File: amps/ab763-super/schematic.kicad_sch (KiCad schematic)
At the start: 113 parts, among them T1 125P5D · 360-0-360V, T2 125C1A, T3 125A9A, T4 125A20B

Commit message: Fix: state the datasheet unit on 17 dual-triode sections whose sheets printed the other half's pin numbers
The sheet-vs-board gate reported these sockets as SECTION-SWAP; the
2026-09-10 source-read triage found the BOARD right on every one of them
(and both surfaces wrong on the 5G9 tremolo bottle). Each sheet had
lettered the section on the default map (A -> unit 1 -> pins 6/7/8) where
the factory drawing puts that stage on 1/2/3. The draw scripts now state
`unit=` on both halves, with the source cited beside the call, so the
printed socket numbers are the factory's:

- 5f4 V3: driver V3A -> 1/2/3, cathodyne V3B -> 6/7/8
  (crop 5f4-V3-layout-trace.png: +213 V driver plate -> pin 1, +270 V -> 6)
- 5f8a V3: 82k half V3A -> 1/2/3, 100k half V3B -> 6/7/8
  (crop 5f8a-V3-layout-trace.png: +225 -> 6, +19 -> 2, +28.5 -> 8)
- 6161 V1: channel 1 V1A -> 1/2/3 (crop 6161-V1-ch1.png prints 1/2/3);
  6161 V2: 1 MEG-grid half V2A -> 1/2/3, paraphase V2B -> 6/7/8
  (crop 6161-V2.png / 6161-V2-right.png)
- 6g3 V3: 82k half V3A -> 1/2/3 (crop 6g3-V3-layout-wires.png: +230 -> 1,
  +225 -> 6, +20 -> 7)
- aa1164 V3: recovery V3A -> 1/2/3, mixer V3B -> 6/7/8
  (crops aa1164-V3A-recovery-schem.png, aa1164-V3B-mixer-schem.png)
- aa864-bassman V1/V2: input stages 2/1/3, second stages 7/6/8; V4: the
  .1/500 pF-fed 82k half 2/1/3 (crops aa864-V1A-input.png,
  aa864-V1B-second.png, aa864-V2A-input.png, aa864-V2B-second.png,
  aa864-V4-PI.png)
- ab165 V1/V2/V4: same pattern (crops ab165-V1A-input.png,
  ab165-V1B-second.png, ab165-V2A-input.png, ab165-V2B-second.png,
  ab165-V4-PI.png)
- ab763-super V1/V2: slope-plate +270 V -> pin 1 (input stage), .047
  plate -> 6 (crops ab763-super-V1-layout-sh.png, ab763-super-V2-layout-sh.png)
- dr103 V2/V3: gain stages 6/7/8, cathode followers 1/2/3 (crops
  dr103-V2-huss.png, dr103-V3-huss.png — the Huss redraw, not a factory
  print; noted in the script)
- 5g9 V3: oscillator V3A -> 1/2/3, follower V3B -> 6/7/8 (crops
  5g9-V3-strap71-zoom.png, 5g9-V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
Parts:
- V1A, V2A: Basing_unit (none) -> 2
- V1B, V2B: Basing_unit (none) -> 1
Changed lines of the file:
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@@
     (in_bom yes) (on_board yes)
     (property "Reference" "V1A" (at 65.6088 33.489 0) (effects (font (size 1.27 1.27)) (justify left)))
-    (property "Value" "12AX7" (at 65.6088 35.889 0) (effects (font (size 1.27 1.27)) (justify left))))
+    (property "Value" "12AX7" (at 65.6088 35.889 0) (effects (font (size 1.27 1.27)) (justify left)))
+    (property "Basing_unit" "2" (at 65.6088 38.289 0) (effects (font (size 1.27 1.27)) hide)))
   (wire (pts (xy 47.6088 39.889) (xy 51.9888 39.889))
     (stroke (width 0) (type default)))
@@
     (in_bom yes) (on_board yes)
     (property "Reference" "V1B" (at 165.609 33.489 0) (effects (font (size 1.27 1.27)) (justify left)))
-    (property "Value" "12AX7" (at 165.609 35.889 0) (effects (font (size 1.27 1.27)) (justify left))))
+    (property "Value" "12AX7" (at 165.609 35.889 0) (effects (font (size 1.27 1.27)) (justify left)))
+    (property "Basing_unit" "1" (at 165.609 38.289 0) (effects (font (size 1.27 1.27)) hide)))
   (wire (pts (xy 147.609 39.889) (xy 151.989 39.889))
     (stroke (width 0) (type default)))
@@
     (in_bom yes) (on_board yes)
     (property "Reference" "V2A" (at 65.6088 87.489 0) (effects (font (size 1.27 1.27)) (justify left)))
-    (property "Value" "12AX7" (at 65.6088 89.889 0) (effects (font (size 1.27 1.27)) (justify left))))
+    (property "Value" "12AX7" (at 65.6088 89.889 0) (effects (font (size 1.27 1.27)) (justify left)))
+    (property "Basing_unit" "2" (at 65.6088 92.289 0) (effects (font (size 1.27 1.27)) hide)))
   (wire (pts (xy 47.6088 93.889) (xy 51.9888 93.889))
     (stroke (width 0) (type default)))
@@
     (in_bom yes) (on_board yes)
     (property "Reference" "V2B" (at 165.609 87.489 0) (effects (font (size 1.27 1.27)) (justify left)))
-    (property "Value" "12AX7" (at 165.609 89.889 0) (effects (font (size 1.27 1.27)) (justify left))))
+    (property "Value" "12AX7" (at 165.609 89.889 0) (effects (font (size 1.27 1.27)) (justify left)))
+    (property "Basing_unit" "1" (at 165.609 92.289 0) (effects (font (size 1.27 1.27)) hide)))
   (wire (pts (xy 147.609 93.889) (xy 151.989 93.889))
     (stroke (width 0) (type default)))
@@
   (polyline (pts (xy 79.7088 238.244) (xy 81.6088 236.644) (xy 87.6088 238.724) (xy 93.6088 236.644) (xy 95.5088 238.244))
     (stroke (width 0.598) (type default) (color 197 163 255 1)) (fill (type none)))
-  (text "6" (at 60.4588 33.539 0)
+  (text "1" (at 60.4588 33.539 0)
     (effects (font (size 1.1 1.1)) (justify left)))
-  (text "7" (at 52.6616 38.489 0)
+  (text "2" (at 52.6616 38.489 0)
     (effects (font (size 1.1 1.1)) (justify left)))
-  (text "8" (at 60.4588 46.239 0)
+  (text "3" (at 60.4588 46.239 0)
     (effects (font (size 1.1 1.1)) (justify left)))
-  (text "1" (at 160.459 33.539 0)
+  (text "6" (at 160.459 33.539 0)
     (effects (font (size 1.1 1.1)) (justify left)))
-  (text "2" (at 152.662 38.489 0)
+  (text "7" (at 152.662 38.489 0)
     (effects (font (size 1.1 1.1)) (justify left)))
-  (text "3" (at 160.459 46.239 0)
+  (text "8" (at 160.459 46.239 0)
     (effects (font (size 1.1 1.1)) (justify left)))
-  (text "6" (at 60.4588 87.539 0)
+  (text "1" (at 60.4588 87.539 0)
     (effects (font (size 1.1 1.1)) (justify left)))
-  (text "7" (at 52.6616 92.489 0)
+  (text "2" (at 52.6616 92.489 0)
     (effects (font (size 1.1 1.1)) (justify left)))
-  (text "8" (at 60.4588 100.239 0)
+  (text "3" (at 60.4588 100.239 0)
     (effects (font (size 1.1 1.1)) (justify left)))
-  (text "1" (at 160.459 87.539 0)
+  (text "6" (at 160.459 87.539 0)
     (effects (font (size 1.1 1.1)) (justify left)))
-  (text "2" (at 152.662 92.489 0)
+  (text "7" (at 152.662 92.489 0)
     (effects (font (size 1.1 1.1)) (justify left)))
-  (text "3" (at 160.459 100.239 0)
+  (text "8" (at 160.459 100.239 0)
     (effects (font (size 1.1 1.1)) (justify left)))
   (text "6" (at 80.4588 137.539 0)

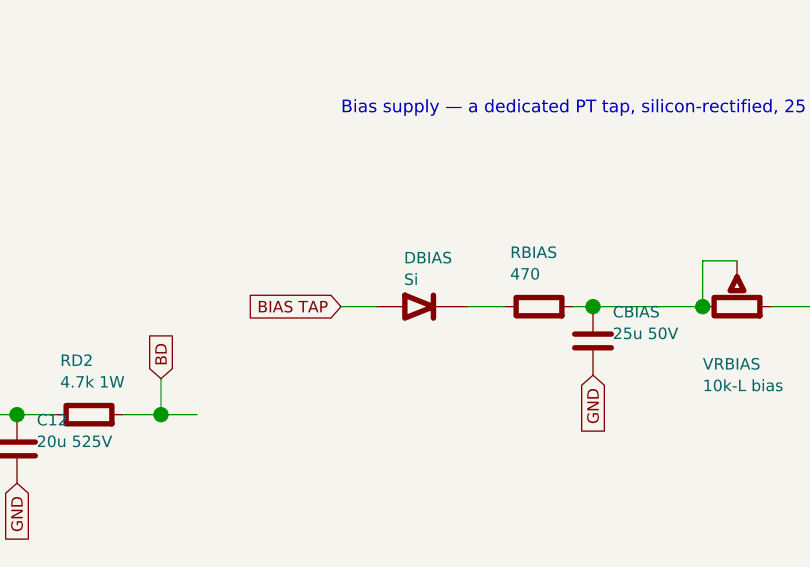
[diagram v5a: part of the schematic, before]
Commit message: Fix: 17 bias rectifiers and six HT diodes drawn backwards; the 6G6-B and 6G4 bias rows as their drawings show; AA1164 V4 units
Rectifier polarity has no gate. The netlists model every supply as an ideal
source, the sheet-vs-board check treats a two-terminal part as unordered, and
the boards' `cathode:` fields were copied from the sheets. Measured over all
68 diodes on 40 sheets: 18 negative-bias rectifiers had the cathode on the
negative node (a diode that way round would charge the node POSITIVE), and all
six 6G6-B HT diodes pointed away from B+. The printed negative bias on each of
those sheets falsifies the drawn orientation; the nine bias rectifiers already
right (AA1164, AA864, AB165, B15N, DR103, JTM100, M1959, M2204, 6G6-B) show
the idiom. Flipped: 5E4-A, 5E5-A, 5E6-A, 5F10, 5F4, 5F6, 5F6-A, 5F8-A, 5G9,
6G2, 6G3, 6G4, 6G5, AA964, AB763, AB763 Super, AB763 Twin, JTM45 (the
M1987's is with the Marshall board repair) and the 6G6-B's DR1-DR6. The
5F8-A board, which had copied its sheet, has the band moved to the tap side;
the other boards' bands are with the board-repair wave. A gate is next.

6G6-B bias. E-FB (6431x3364): the 1K 1W rises from TR1's SECOND secondary
terminal, a bias tap between the upper HT end and the grounded centre tap,
to the diode's + end. The sheet fed the diode from the HT end with the 1K
after it. T1 now carries its tap pin and the row reads tap -> 1K -> diode ->
-54 V. (The triage had read "HT end"; the native crop shows the tap.)

6G4 bias. A-FJ, read natively: tap -> rectifier -> 8 uF -> 10K -> the -55 V
node, which carries a second 8 uF and the 56K to ground as a bleeder. The
sheet fed the rectifier from an HT end, drew the 56K in series and carried
one capacitor. CBIAS2 joins the parts list, and RBIAS1's role now says
bleeder.

AA1164 V4. The K-FD sheet prints the phase inverter 7/6/8 and the tremolo
oscillator 2/1/3 (5554x4346); the sheet had them the other way round.

Gates: check_schematics 40/0 (+selftest), verify_schematic_nets 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
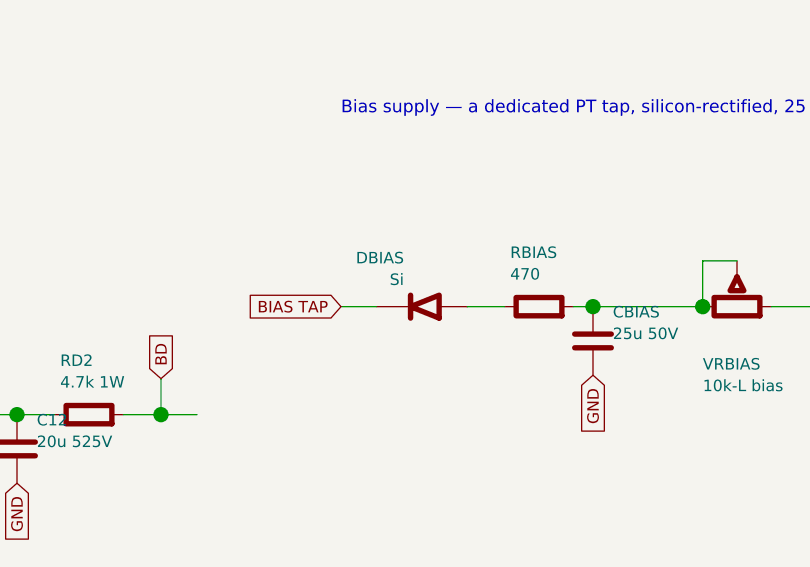
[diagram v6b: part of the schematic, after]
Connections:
- net BIAS TAP: now also DBIAS.2 (K); no longer DBIAS.1 (A)
- net at RBIAS.1: now also DBIAS.1 (A); no longer DBIAS.2 (K)
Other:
- moved on the sheet: DBIAS
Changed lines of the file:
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@@
   (wire (pts (xy 225.609 233.889) (xy 229.529 233.889))
     (stroke (width 0) (type default)))
-  (symbol (lib_id "cx:DIODE_SS") (at 234.609 233.889 0) (unit 1)
+  (symbol (lib_id "cx:DIODE_SS") (at 234.609 233.889 180) (unit 1)
     (in_bom yes) (on_board yes)
     (property "Reference" "DBIAS" (at 232.609 228.489 0) (effects (font (size 1.27 1.27)) (justify left)))

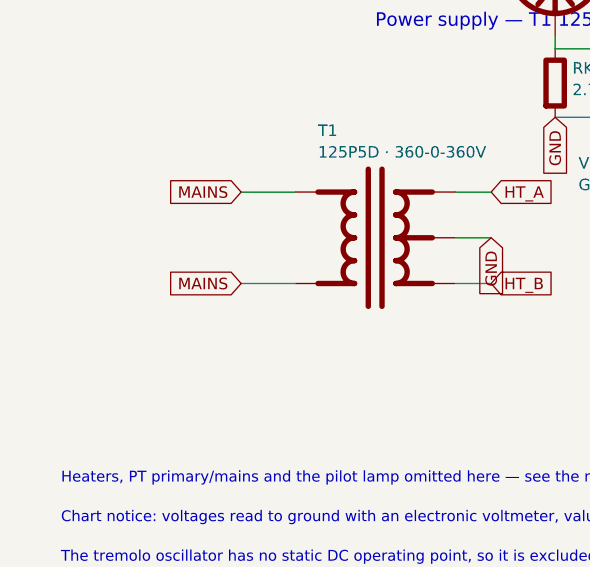
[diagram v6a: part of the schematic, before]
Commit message: Fix: the 6G5's rectifier was connected to nothing; 17 sheets shorted the mains by naming both leads alike
6G5 power supply. The sheet drew four diodes as a "silicon bridge" whose
HT_A/HT_B labels stopped 6 mm short of their wires. D1/D2's anodes sat on
the tremolo's cathode node (a tremolo wire's end touched the old diode
stub), D3/D4 ran from ground to the reservoir, and TR1's centre tap floated
under an open-pin waiver whose stated reason was the bridge itself.
A-FJ (Schematic Heaven 2153x1437, read enlarged): each HT end of TR1 runs
through a leg of three silicon diodes, every + (cathode) toward the +460 V
reservoir; the centre tap is grounded; TR1's second secondary terminal is a
bias tap feeding the 6G4's network part for part: rectifier, 8-150, 10K,
then 8-150 and a 56K bleeder at the -55 V line. Redrawn as the drawing
shows: D1-D6, TR1 with its tap pin, the centre tap to ground, the bias
network (CBIAS 25 uF -> 8 uF; RBIAS2, CBIAS2, RBIAS1 added), the waiver
deleted, and the notes, meta, netlist header and parts list no longer say
bridge. Not yet carried: the drawing's second 20-600 at the reservoir and
the standby switch (this sheet omits chassis switches by its own note);
and the tremolo ladder still runs through the transformer's corner of the
sheet, a layout clash rather than a connection, queued for its own redraw.

Mains. Two global labels with one name are one net. 16 of 24 power
transformers on the sheets carried a label named MAINS on both primary
leads, so the winding's two pins were one net: 5E4-A, 5E5-A, 5F4, 5G9,
6161, 6G2, 6G3, 6G4, AA1164, AA764, AA764-Vibro, AA964, AB763, AB763
Super, AB763 Twin, GA-40. The 6G5's loop ran from one MAINS label through
switch, fuse and winding back to the same name. No gate models the primary,
so a copy-pasted idiom did this. The second lead is now MAINS N, the AC15's
idiom; the AA1164's and AA964's second AC row, drawn under the first row's
name, is the neutral. The death and across-the-line caps stay on the le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
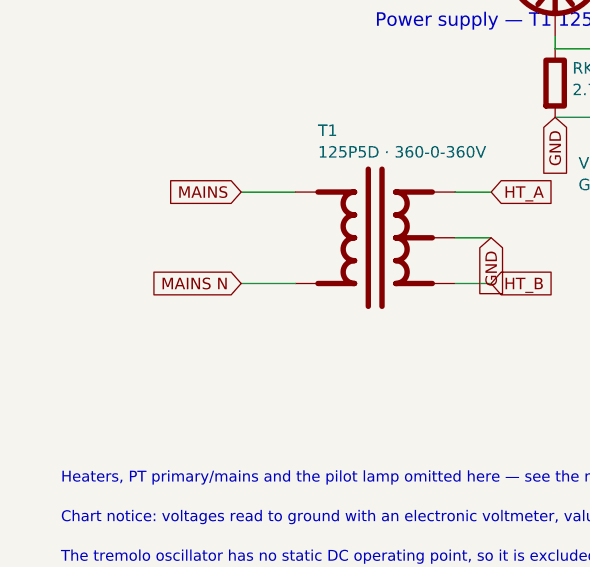
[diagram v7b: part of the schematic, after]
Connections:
- net MAINS: no longer T1.2 (PRI_2)
- new net MAINS N: T1.2 (PRI_2)
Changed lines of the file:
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@@
   (wire (pts (xy 38.7188 242.969) (xy 32.7188 242.969))
     (stroke (width 0) (type default)))
-  (global_label "MAINS" (shape input) (at 32.7188 242.969 180)
+  (global_label "MAINS N" (shape input) (at 32.7188 242.969 180)
     (effects (font (size 1.27 1.27)) (justify right)))
   (wire (pts (xy 56.4988 232.809) (xy 60.4988 232.809))

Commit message: Fix: AB763 Super mixer, reverb send, tremolo (both V5 halves) and bias pot drawn as the C-FD sheet draws them
Read against the SUPER-REVERB-AMP AB763 drawing at 3299 x 2551:
- Dry path: V2B -> .02 -> dry node -> 3.3M || 10PF IN SERIES -> V3A grid.
  The sheet had RGD1 3.3M as a grid leak to ground and CBD1 10p from the grid
  to the PLATE. Its MIXG label at the grid block also stopped 4 mm short of
  its wire, so the dry path never reached the grid.
- The 500PF reverb send leaves the dry node, after the .02. The sheet took it
  off the V2B plate.
- V3A grid: the 470K reverb return and the 220K to ground land there (MIXG).
- V3A output: .1 -> node X -> 220K -> the phase-inverter input junction (where
  the Normal channel's 220K lands) -> .001 -> PI grid. The sheet had CCD1
  lettered .001 straight to the junction, with no 220K. CCD1 is now .1 and
  RMIXV 220k is new.
- Photocell: the 50K-RA Intensity control hangs from node X to ground, and the
  photocell runs from its wiper to ground. The sheet put the photocell on the
  mix driver's grid.
- V5 is a 12AX7 with BOTH halves in use. V5A is the oscillator (+280 V /
  +2.5 V) on the ladder plate -> .02 -> Speed node (3M-RA + 100K to ground)
  -> .01 -> N1 -> .01 -> grid; 1M from N1 and 1M from the grid meet at the
  footswitch junction, which returns through 2.2M to the bias filter node.
  V5B is the lamp driver: grid on N1, 100K || 25 cathode (+17.0 V), 10M from
  the plate to +460, and the neon lamp + 100K to +460 (+390 V at the plate).
  The sheet drew one triode, a two-cap ladder to a grounded 1M, and an
  Intensity rheostat plus a 27k in series with the lamp off the oscillator's
  plate.
- That 27K is the bias pot's leg. The 10K-L track runs from the bias filter
  node to 27K to ground, and its wiper is the -52 V line. The sheet drew the
  pot as a rheostat in series with the line. RINT is gone; RBIAS2 27k is new.
- netlist.cir: the mix driver's DC grid return is now RMR2 220k to ground. It
  was RGD1 3.3M to groun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
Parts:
- removed C2: .1u 400V, symbol cx:C
- removed CPIB: .1u 200V, symbol cx:C
- removed RGPB, RTOG: 1M, symbol cx:R
- removed RINT: 27k, symbol cx:R
- removed RTAIL: 470, symbol cx:R
- removed T3: 125A9A, symbol cx:OT_PP
- removed V5: 12AX7, symbol cx:TRIODE
- added CKTO2: 25u, symbol cx:C
- added CPIA: .001u, symbol cx:C
- added CTO3: .01u, symbol cx:C
- added RBIAS2: 27k, symbol cx:R
- added RBL1: 220k 1W, symbol cx:R
- added RGL1: 220k 5%, symbol cx:R
- added RKTO2: 100k, symbol cx:R
- added RLPA: 82k 5%, symbol cx:R
- added RMIXV: 220k, symbol cx:R
- added RST1: 1.5k, symbol cx:R
- added RT2: 22k, symbol cx:R
- added RTO10: 10M, symbol cx:R
- added RTOG1: 1M, symbol cx:R
- added RTOG3: 2.2M, symbol cx:R
- added T1: 125P5D · 360-0-360V, symbol cx:PT
- added V5B: 12AX7, symbol cx:TRIODE
- added VRINT: 50k-RA int, symbol cx:POT
- C2: renamed from RT2; value 22k -> .1u 400V; symbol cx:R -> cx:C
- CCD1: value .001u -> .1u
- CPIB: renamed from RLPA; value 82k 5% -> .1u 200V; symbol cx:R -> cx:C
- CTO1: value .01u -> .02u
- RGPB: renamed from CPIA; value .001u -> 1M; symbol cx:C -> cx:R
- RLAMP: renamed from RBL1; value 220k 1W -> 100k
- RTAIL: renamed from VRINT; value 50k-RA int -> 470; symbol cx:POT -> cx:R
- RTOG2: renamed from T1; value 125P5D · 360-0-360V -> 1M; symbol cx:PT -> cx:R
- T3: renamed from RGL1; value 220k 5% -> 125A9A; symbol cx:R -> cx:OT_PP
- V5A: renamed from RST1; value 1.5k -> 12AX7; symbol cx:R -> cx:TRIODE
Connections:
- net -52V: now also VRBIAS.2 (W), RGL1.1; no longer T3.1, VRBIAS.3
- net BC: now also RLPA.1; no longer CPIB.1
- net BP1: now also RLAMP.2, T3.2 (CT), RTO10.1
- net GND: now also T3.5 (SEC_C), CKTO2.2, RBIAS2.2, RBL1.2, RKTO2.2, RT2.2, T1.4 (HT_CT), VRINT.3; no longer C2.2, CTO2.1, OPTO.2 (L2), RGD1.2, RLAMP.2, RTOG2.4 (HT_CT)
- net HT_A: now also T1.3 (HT_A); no longer RTOG2.3 (HT_A)
- net HT_B: now also T1.5 (HT_B); no longer RTOG2.5 (HT_B)
- net MAINS: now also T1.1 (PRI_1); no longer RTOG2.1 (PRI_1)
- net MAINS N: now also T1.2 (PRI_2); no longer RTOG2.2 (PRI_2)
- net MIXG: now also CBD1.2, RGD1.2, RMR2.1, V3A.2 (G); no longer CCV2.2, OPTO.3 (P1)
- net PIG: now also CPIA.1, RMIXV.2; no longer CCD1.2, RGPB.1
- net SPKR: now also T3.4 (SEC_H)
- net at C2.1: now also RLPB.2, V6B.1 (P); no longer RGPA.2
- net at V6B.2 (G): now also CPIB.2, RGPB.2
- net at RGL2.1, RST2.1: now also C2.2
- net DRY: now reaches CBD1.1, RGD1.1
- net DRY: now also CCV2.2, CRS.2; no longer RMR2.1, V3A.2 (G)
- net at CTO1.1, RTO2.2: now also V5A.1 (P); no longer RTAIL.1, RTAIL.2 (W)
- net at CCV2.1, RLV2.2, V2B.1 (P): no longer CRS.2
- net BIAS FILTER: now reaches CBIAS.1, RBIAS.2, VRBIAS.1
- net BIAS FILTER: now also RTOG3.2; no longer VRBIAS.2 (W)
- net at CKTO1.1, RKTO1.1: now also V5A.3 (K)
- net at C10.1, RBL2.1, T2.1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: now also RBL1.1; no longer RLAMP.1
- net at CCD1.1, RLD1.2, V3A.1 (P): no longer CBD1.2
- net at V7.1 (P): now also T3.1 (PRI_A)
- net at V7.2 (G1): now also RST1.2; no longer V5A.2
- net at OPTO.1 (L1): now also RTO10.2, V5B.1 (P)
- net at RGPA.1, V6A.2 (G): now also CPIA.2; no longer RGPB.2
- net at C1.1, V6A.1 (P): now also RLPA.2; no longer CPIB.2
- net at V6A.3 (K), V6B.3 (K): now also RTAIL.2
- net at V8.1 (P): now also T3.3 (PRI_B)
- net at RNFB.2: now also CPIB.1
- new net: RBIAS2.1, VRBIAS.3
- new net: C1.2, RGL1.2, RST1.1
- new net: RGPA.2, RGPB.1, RT2.1, RTAIL.1
- new net: CCD1.2, RMIXV.1, VRINT.1
- new net: OPTO.2 (L2), RLAMP.1
- new net: CTO2.1, CTO3.1, RTOG1.2, V5B.2 (G)
- new net: CKTO2.1, RKTO2.1, V5B.3 (K)
- new net: RTOG1.1, RTOG2.1, RTOG3.1
- new net: CTO3.2, RTOG2.2, V5A.2 (G)
- new net PHOTOCELL: OPTO.3 (P1), VRINT.2 (W)
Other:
- note added: "Bias supply — PT tap, silicon rectifier, 25 µF filter; 10 kΩ-L pot over a 27 kΩ leg, wiper to -52 V"
- note added: "Neither tremolo half has a static DC operating point, so V5 is excluded from the netlist (see the circuit story); both halves tap BP1 directly, a driven node, so excluding them moves no gated node."
- note added: "The vibrato footswitch grounds the junction of the two 1 MΩ ladder resistors and the 2.2 MΩ, and stops the oscillator (the pedal jack is not drawn here)"
- note added: "Tremolo — oscillator V5A and neon-lamp driver V5B; neither half has a static DC operating point, so both are excluded from the netlist (see the circuit story)"
- note removed: "Bias supply — a dedicated PT tap, silicon-rectified, 25 µF-filtered, through an adjustable 10 kΩ-L pot"
- note removed: "The tremolo oscillator has no static DC operating point, so it is excluded from the netlist (see the circuit story); its supply taps BP1 directly, a driven node, so excluding it moves no gated node."
- note removed: "The vibrato footswitch grounds the oscillator grid bus and stops the oscillator (period detail; not modelled here)"
- note removed: "Tremolo oscillator (V5, one 12AX7 half) — excluded from the netlist (see the circuit story)"
- moved on the sheet: RLAMP
